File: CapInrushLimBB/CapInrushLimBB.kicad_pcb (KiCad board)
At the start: 2 copper layers, 56.5 x 34.9 mm, 29 parts, among them J1 Screw_Terminal_01x02, J2 Screw_Terminal_01x02, K1 G5LE-1A, Q1 MPSA42, Q2 IRF9540N, Q3 MPSA42, Q4 BSP230 300V 0.21A

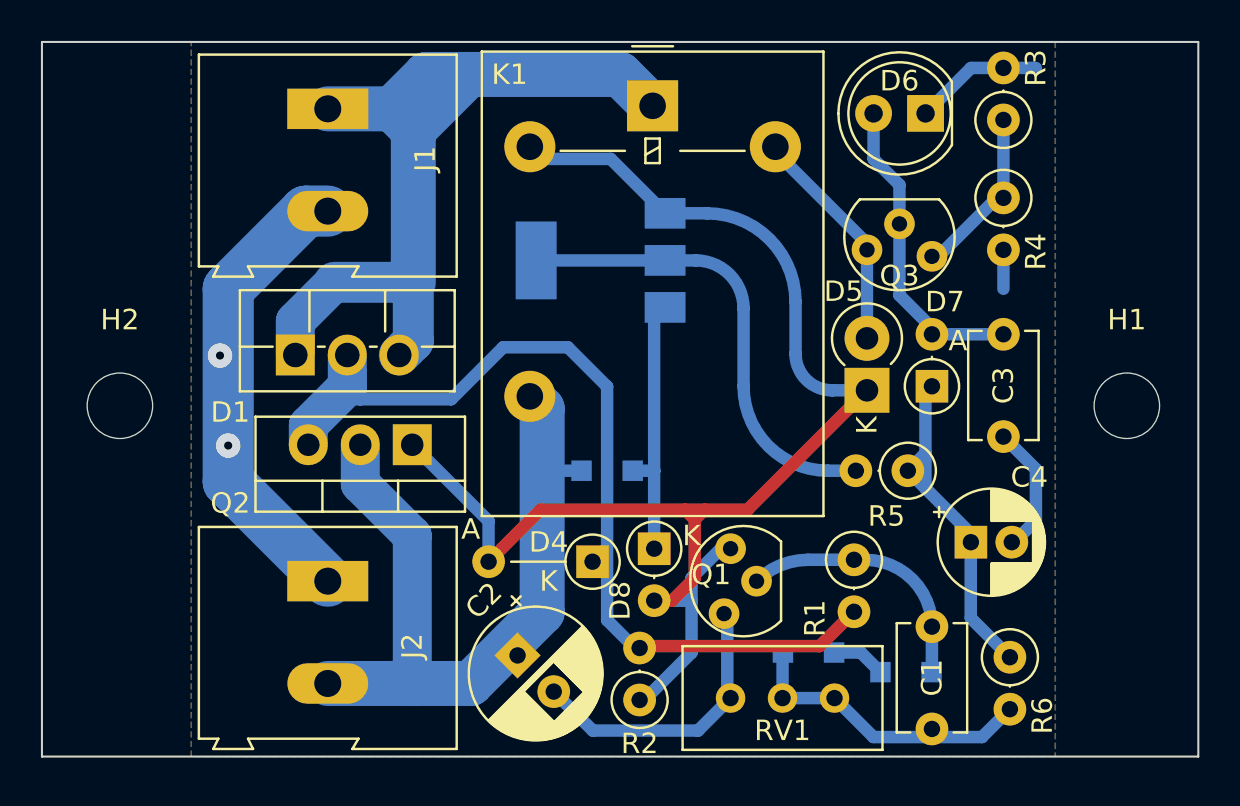
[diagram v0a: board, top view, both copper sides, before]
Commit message: Modified schematic to support low voltage operation with 24V relay and updated board layout.
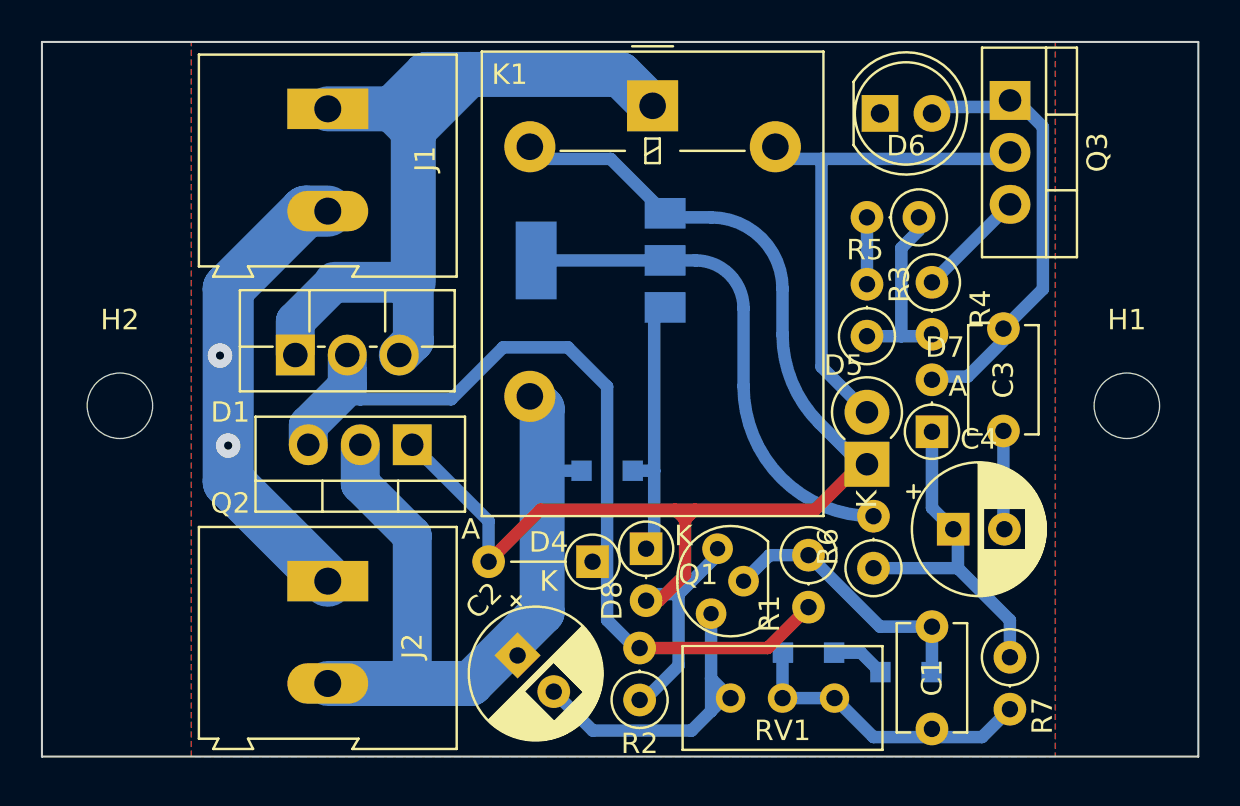
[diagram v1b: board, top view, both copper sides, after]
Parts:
- added R4: 0R, Resistor_THT:R_Axial_DIN0207_L6.3mm_D2.5mm_P2.54mm_Vertical, F.Cu at (250.5, 137.2)
- C4: value 10uF 63V -> 100uF 35V; footprint Capacitor_THT:CP_Radial_D5.0mm_P2.00mm -> Capacitor_THT:CP_Radial_D6.3mm_P2.50mm
- Q3: value MPSA42 -> TIP41C; footprint CapInrushLim:TO-92_Inline -> Package_TO_SOT_THT:TO-220-3_Vertical
- R1: value 100k -> 43k
- R3: value 1k5 -> 220R
- R5: renamed from R4; value 100R -> 110R
- R6: renamed from R5; value 100k -> 10k
- R7: renamed from R6; value 200k -> 100k
- moved R3 12.5 mm to (247.3, 139.8)
- moved Q3 7.85 mm to (254.3, 128.3), turned to -90 degrees
- moved R6 5.05 mm to (247.7, 151.1), turned to 90 degrees
- moved R5 4.24 mm to (249.9, 134.0), turned to 180 degrees
- moved D5 3.61 mm to (247.3, 146.1)
- moved R1 2.23 mm to (244.5, 150.5)
- moved D6 2.23 mm to (248.0, 128.9), turned to 0 degrees
- moved D7 2.22 mm to (250.5, 144.5)
- moved C4 1.07 mm to (251.5, 149.2)
- moved Q1 0.64 mm to (240.7, 153.0)
- moved D8 0.40 mm to (236.5, 150.2)
- moved C3 0.28 mm to (254.0, 144.4)
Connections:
- Q3 pad 1: Net-(Q3-Pad1) -> Net-(C3-Pad2)
- Q3 pad 2: Net-(C3-Pad2) -> /RLCoilLow
- Q3 pad 3: /RLCoilLow -> Net-(Q3-Pad3)
- R3 pad 1: Net-(Q3-Pad1) -> Net-(R3-Pad1)
- R5 pad 1: Net-(Q3-Pad1) -> Net-(R3-Pad1)
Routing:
- net /RLCoilLow: track 11.2 -> 25.2 mm
- net Net-(R3-Pad1): track 0.00 -> 8.74 mm
- net Net-(Q3-Pad1): track 8.49 -> 0.00 mm
- net /Gnd: track 52.1 -> 45.5 mm
- net Net-(C3-Pad2): track 14.8 -> 20.8 mm
- net Net-(Q3-Pad3): track 0.00 -> 5.40 mm
- net /PolProtect: track 47.3 -> 45.2 mm
- net Net-(Q4-Pad2): track 22.9 -> 24.9 mm
- net Net-(C2-Pad2): track 14.3 -> 16.2 mm
- net /RLCoilHigh: track 70.6 -> 69.7 mm
- net Net-(C1-Pad1): track 12.8 -> 13.4 mm

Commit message: Updated PCB layout of lower voltage capable inrush limiter.
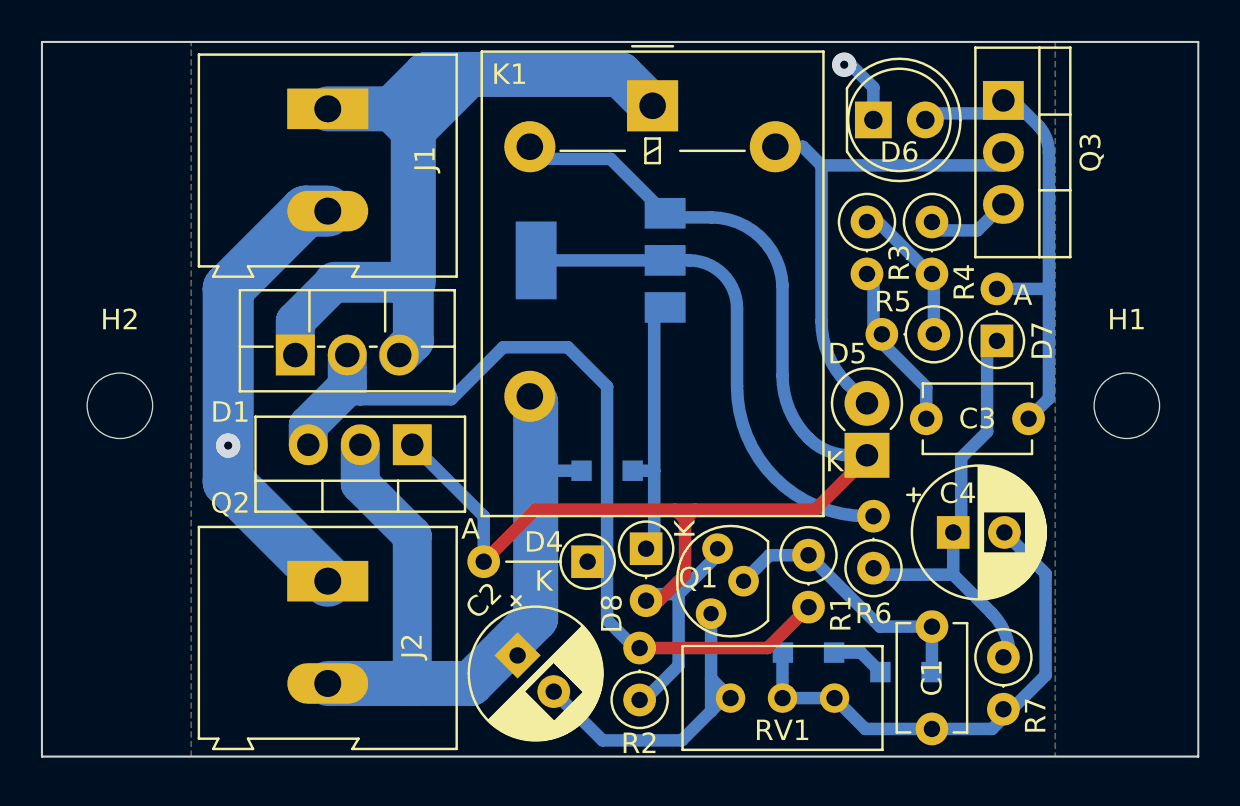
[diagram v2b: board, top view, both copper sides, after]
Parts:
- moved R5 5.76 mm to (250.6, 139.7)
- moved R3 5.58 mm to (247.3, 134.2), turned to -90 degrees
- moved D7 5.46 mm to (253.7, 140.0)
- moved C3 3.82 mm to (250.2, 143.8), turned to 0 degrees
- moved R4 2.95 mm to (250.5, 134.2)
- moved D6 0.45 mm to (247.6, 129.2)
- moved D5 0.44 mm to (247.3, 145.6)
- moved Q3 0.32 mm to (254.0, 128.3)
- moved R7 0.32 mm to (254.0, 155.5)
- moved D4 0.24 mm to (233.7, 150.8)
- moved C4 0.16 mm to (251.5, 149.4)
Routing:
- net /Gnd: track 45.5 -> 58.7 mm
- net Net-(C4-Pad1): track 16.9 -> 21.2 mm
- net Net-(C3-Pad2): track 20.8 -> 23.4 mm
- net Net-(R3-Pad1): track 8.74 -> 6.99 mm
- net /RLCoilHigh: track 69.7 -> 71.3 mm
- net Net-(Q3-Pad3): track 5.40 -> 4.43 mm
- net /RL_Output: track 36.1 -> 36.9 mm
- net /RLCoilLow: track 25.2 -> 24.5 mm

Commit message: Added lower voltage tollerant model and started tweaking PCB layout to move pass element somewhere where it can be heat sunk.
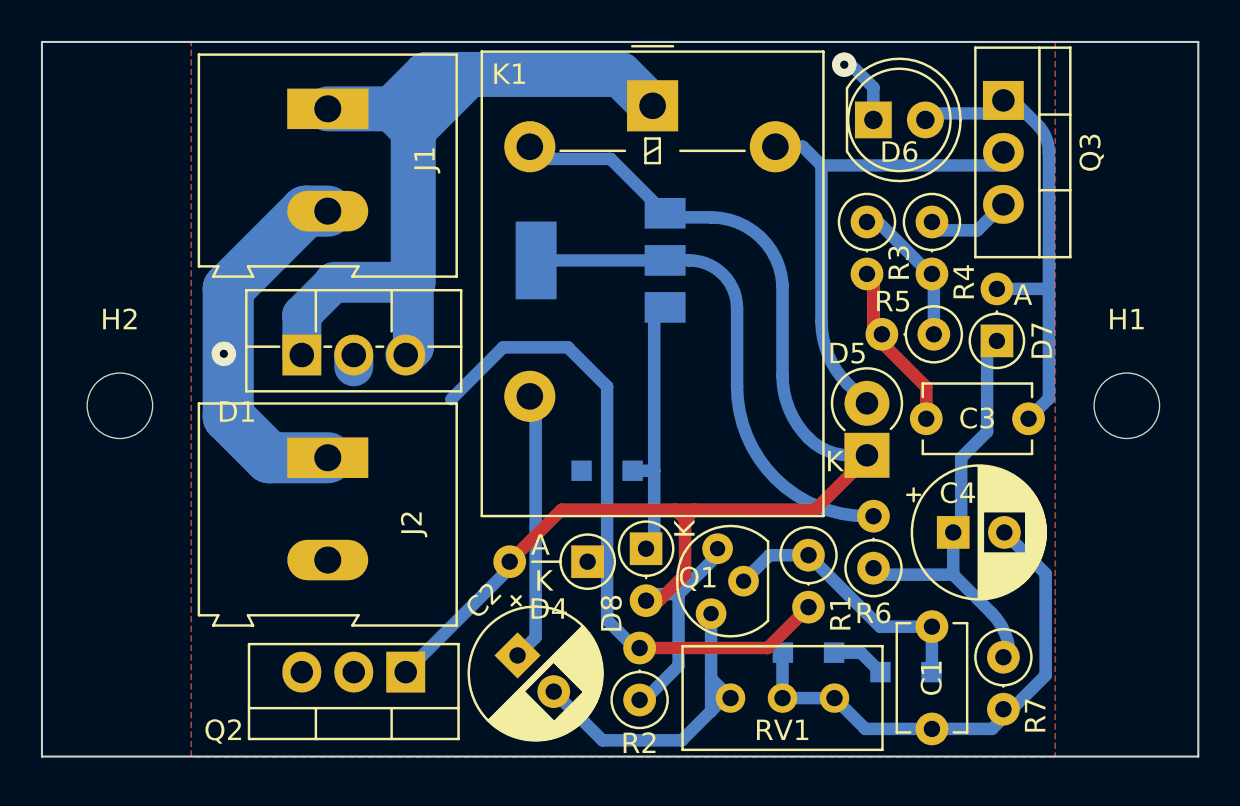
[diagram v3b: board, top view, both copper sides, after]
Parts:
- D4: footprint Diode_THT:D_DO-35_SOD27_P5.08mm_Vertical_AnodeUp -> Diode_THT:D_DO-35_SOD27_P3.81mm_Vertical_AnodeUp
- moved Q2 11.1 mm to (224.8, 156.2)
- moved J2 6.03 mm to (221.0, 145.7)
- moved D1 0.32 mm to (219.7, 140.7)
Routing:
- net /RL_Output: track 36.9 -> 13.1 mm
- net /PolProtect: track 45.2 -> 32.7 mm
- net /Gnd: track 58.7 -> 57.3 mm
- net /RLCoilHigh: track 71.3 -> 70.4 mm

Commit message: Updated footprints in schematic and layed out tracks to make pass element accessable from the side of the board.
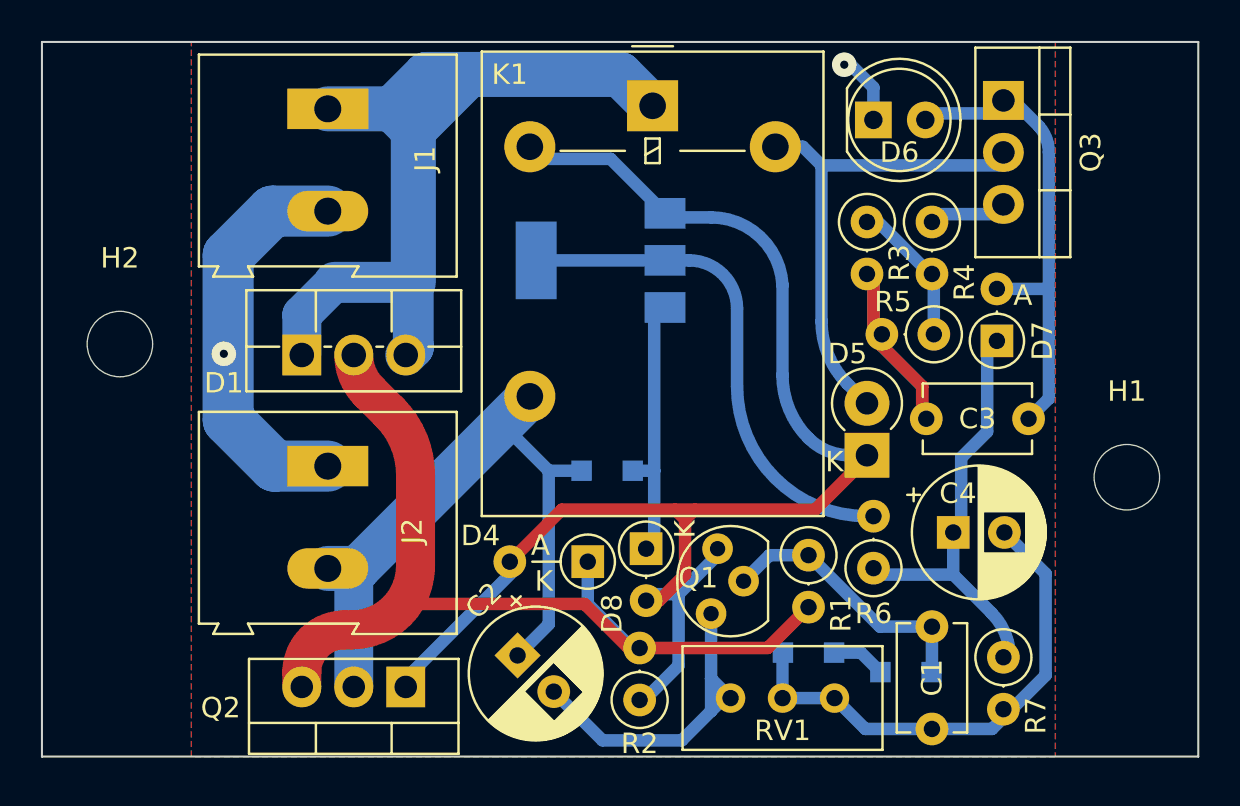
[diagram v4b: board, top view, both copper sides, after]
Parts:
- moved H1 3.49 mm to (260.0, 146.7)
- moved H2 3.02 mm to (210.8, 140.2)
- moved Q2 0.72 mm to (224.8, 156.9)
- moved J2 0.41 mm to (221.0, 146.1)
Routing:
- net /RL_Output: track 13.1 -> 33.4 mm
- net /PolProtect: track 32.7 -> 47.2 mm
- net /Gnd: track 57.3 -> 63.4 mm
- net Net-(Q3-Pad3): track 4.43 -> 3.50 mm
- net /RLCoilHigh: track 70.4 -> 71.0 mm
- net Net-(C3-Pad2): track 23.4 -> 22.7 mm
